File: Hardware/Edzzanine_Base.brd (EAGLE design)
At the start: 30.5 x 44.5 mm, 46 parts, among them U2 FTS31XS-U, U4 TPS62065

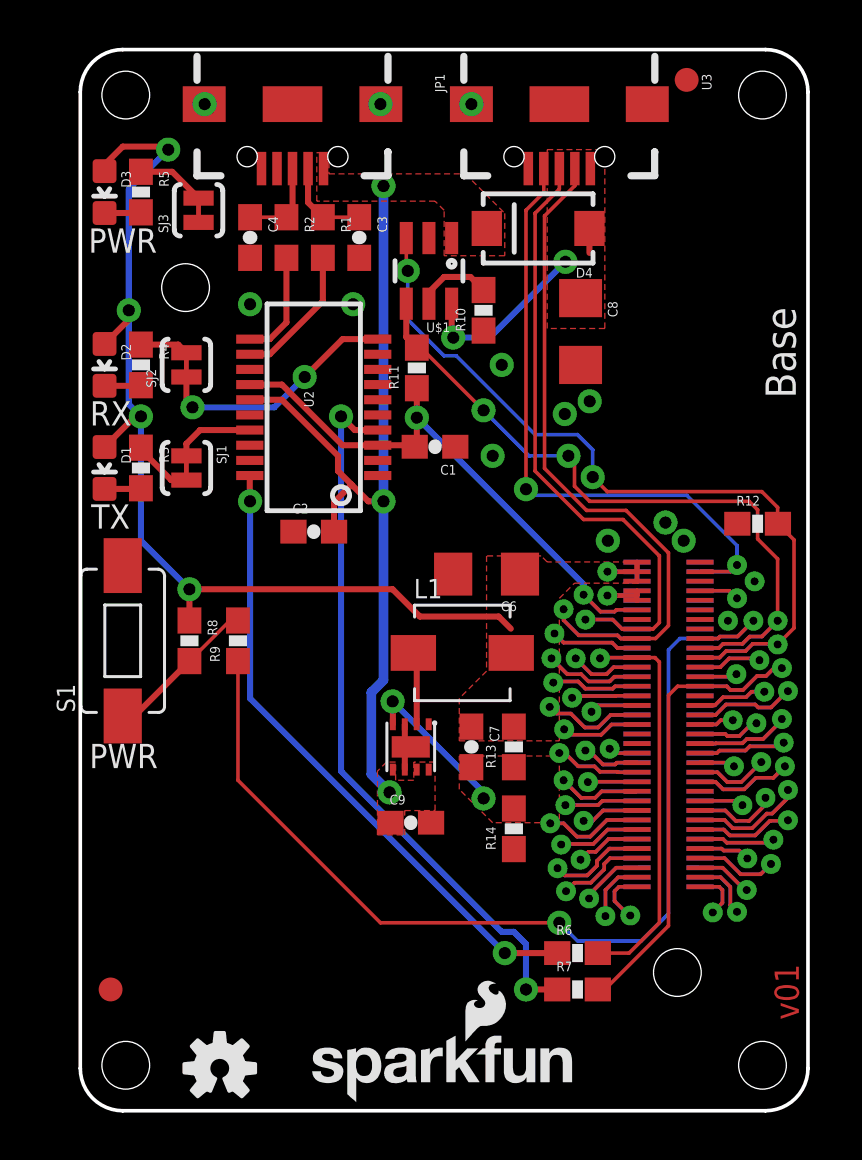
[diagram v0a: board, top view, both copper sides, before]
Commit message: Corrected OTG power issue Corrected name and position added DCIN pin to connector Added DCIN enable circuit corrected dimensions and cleaned up drawings replaced power button with new SMD side shooting button.
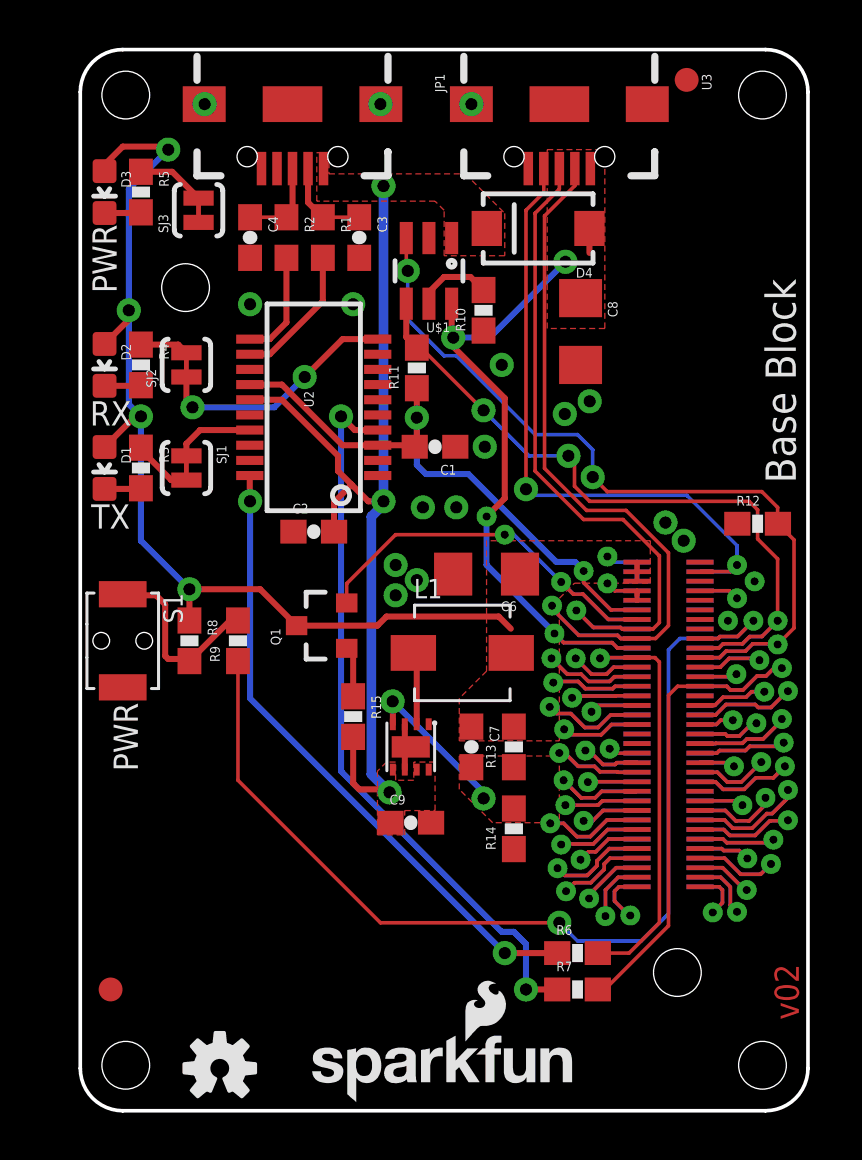
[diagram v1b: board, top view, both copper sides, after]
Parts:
- added Q1: BSS138, SparkFun-DiscreteSemi:SOT23-3
- added R15: 1K, SparkFun-Resistors:0603-RES
- R9: value 22 -> 220
- S1: device SparkFun-Electromechanical:TACTILE-SWITCH-1101NE -> SparkFun-Electromechanical:TACTILE_SWITCH-SMD-RIGHT-ANGLE
- turned S1 to 270 degrees
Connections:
- new net DCIN: E1.14, Q1.2, U$3.14
- net 5V: now also R15.2
- net GND: now also S1.2; no longer S1.P$2
- net N$15: now also S1.1; no longer S1.P$1
- net N$18: now also Q1.1, R15.1; no longer C8.1, D4.A, U$1.6, U3.VBUS1
- net USB_VBUS: now also C8.1, D4.A, U$1.6, U3.VBUS1
- net VSYS: now also Q1.3
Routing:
- net USB_VBUS: track 7.42 -> 30.7 mm, vias 1 -> 4
- net DCIN: track 0.00 -> 19.1 mm, vias 0 -> 2
- net N$18: track 8.49 -> 2.12 mm, vias 2 -> 0
- net 5V: track 35.9 -> 39.6 mm
- net 1.8V: track 25.9 -> 27.7 mm
- net N$15: track 6.48 -> 7.95 mm
- net USB_DP: track 28.3 -> 29.3 mm
- net VSYS: track 47.3 -> 46.4 mm
- net USB_DN: track 32.0 -> 32.7 mm
- net GND: vias 14 -> 18
- added copper zone on layer 1, net USB_VBUS
- removed copper zone on layer 1, net N$18
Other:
- board text added: "Base Block"
- board text added: "NOTE: Units are in Inches"
- board text added: "v02"
- board text removed: "Base"
- board text removed: "Connectors Go Here"
- board text removed: "LED's and selector switches go here"
- board text removed: "Max Board Length"
- board text removed: "Nothing goes here... I mean it."
- board text removed: "v01"
